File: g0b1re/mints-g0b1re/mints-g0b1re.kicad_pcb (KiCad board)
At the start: 2 copper layers, 2 parts

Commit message: Board updates
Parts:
- removed REF**: PinHeader_1x04_P2.54mm_Vertical, Connector_PinHeader_2.54mm:PinHeader_1x04_P2.54mm_Vertical
- removed REF**: TestPoint_Pad_D1.0mm, TestPoint:TestPoint_Pad_D1.0mm
- added C1: 10n, Capacitor_SMD:C_0603_1608Metric, F.Cu at (163.8, 153.3)
- added C10: 1u, Capacitor_SMD:C_0603_1608Metric, F.Cu at (163.8, 163.3)
- added C101: 1u, Capacitor_SMD:C_0603_1608Metric, F.Cu at (190.7, 142.8)
- added C102: 10u, Capacitor_SMD:C_0603_1608Metric, F.Cu at (190.7, 146.3)
- added C103: 1u, Capacitor_SMD:C_0603_1608Metric, F.Cu at (190.7, 149.8)
- added C104: 1u, Capacitor_SMD:C_0603_1608Metric, F.Cu at (194.7, 149.8)
- added C11: 10u, Capacitor_SMD:C_0603_1608Metric, F.Cu at (195.5, 118.6)
- added C12: 22u, Capacitor_SMD:C_0603_1608Metric, F.Cu at (189.0, 119.8)
- added C13: 0.1u, Capacitor_SMD:C_0603_1608Metric, F.Cu at (186.5, 115.2)
- added C14: 22u, Capacitor_SMD:C_0603_1608Metric, F.Cu at (198.5, 118.6)
- added C15: 0.1u, Capacitor_SMD:C_0603_1608Metric, F.Cu at (161.8, 108.9)
- added C16: 10n, Capacitor_SMD:C_0603_1608Metric, F.Cu at (163.8, 165.8)
- added C17: 10n, Capacitor_SMD:C_0603_1608Metric, F.Cu at (163.8, 168.3)
- added C18: 10n, Capacitor_SMD:C_0603_1608Metric, F.Cu at (163.8, 170.9)
- added C19: 10n, Capacitor_SMD:C_0603_1608Metric, F.Cu at (163.8, 173.4)
- added C2: 10n, Capacitor_SMD:C_0603_1608Metric, F.Cu at (163.8, 155.8)
- added C20: 22u, Capacitor_SMD:C_0603_1608Metric, F.Cu at (197.6, 173.3)
- added C3: 10n, Capacitor_SMD:C_0603_1608Metric, F.Cu at (163.8, 158.3)
- added C4: 10n, Capacitor_SMD:C_0603_1608Metric, F.Cu at (163.8, 160.8)
- added C5: 0.1u, Capacitor_SMD:C_0603_1608Metric, F.Cu at (164.3, 113.1)
- added C6: 0.1u, Capacitor_SMD:C_0603_1608Metric, F.Cu at (164.3, 107.1)
- added C7: 0.1u, Capacitor_SMD:C_0603_1608Metric, F.Cu at (161.8, 105.9)
- added C8: 1n, Capacitor_SMD:C_0603_1608Metric, F.Cu at (163.8, 126.0)
- added C9: 0.1u, Capacitor_SMD:C_0603_1608Metric, F.Cu at (166.8, 135.5)
- added D1: 3.3v, LED_SMD:LED_0603_1608Metric, F.Cu at (141.1, 76.3)
- added D101: 1SS396, Package_TO_SOT_SMD:SOT-23, F.Cu at (208.5, 187.2)
- added D102: 1SS396, Package_TO_SOT_SMD:SOT-23, F.Cu at (203.6, 187.2)
- added D103: 1SS396, Package_TO_SOT_SMD:SOT-23, F.Cu at (195.7, 187.2)
- added D104: 1SS396, Package_TO_SOT_SMD:SOT-23, F.Cu at (190.5, 187.2)
- added D105: 1SS396, Package_TO_SOT_SMD:SOT-23, F.Cu at (178.9, 187.2)
- added D106: 1SS396, Package_TO_SOT_SMD:SOT-23, F.Cu at (183.9, 187.2)
- added D107: 1SS396, Package_TO_SOT_SMD:SOT-23, F.Cu at (170.3, 187.2)
- added D108: 1SS396, Package_TO_SOT_SMD:SOT-23, F.Cu at (165.3, 187.2)
- added D2: LED, LED_SMD:LED_0603_1608Metric, F.Cu at (161.8, 114.9)
- added D201: SMBJ5360B-TP, Diode_SMD:D_SMB, F.Cu at (237.7, 85.1)
- added D202: SMBJ5360B-TP, Diode_SMD:D_SMB, F.Cu at (237.7, 119.1)
- added D203: SMBJ5360B-TP, Diode_SMD:D_SMB, F.Cu at (237.7, 151.8)
- added D204: SMBJ5360B-TP, Diode_SMD:D_SMB, F.Cu at (237.7, 185.3)
- added D205: red, LED_SMD:LED_0603_1608Metric, F.Cu at (197.1, 68.4)
- added D206: red, LED_SMD:LED_0603_1608Metric, F.Cu at (197.1, 71.2)
- added D207: red, LED_SMD:LED_0603_1608Metric, F.Cu at (197.1, 74.3)
- added D208: red, LED_SMD:LED_0603_1608Metric, F.Cu at (197.1, 77.3)
- added D209: red, LED_SMD:LED_0603_1608Metric, F.Cu at (201.0, 68.4)
- added D210: red, LED_SMD:LED_0603_1608Metric, F.Cu at (201.0, 71.3)
- added D211: red, LED_SMD:LED_0603_1608Metric, F.Cu at (201.0, 74.4)
- added D212: red, LED_SMD:LED_0603_1608Metric, F.Cu at (201.0, 77.4)
- added D213: SMBJ5360B-TP, Diode_SMD:D_SMB, F.Cu at (251.7, 97.8)
- added D214: SMBJ5360B-TP, Diode_SMD:D_SMB, F.Cu at (251.7, 131.6)
- added D215: SMBJ5360B-TP, Diode_SMD:D_SMB, F.Cu at (251.7, 163.8)
- added D216: SMBJ5360B-TP, Diode_SMD:D_SMB, F.Cu at (251.7, 197.3)
- added D217: red, LED_SMD:LED_0603_1608Metric, F.Cu at (141.1, 68.8)
- added D3: GREEN, LED_SMD:LED_0603_1608Metric, F.Cu at (183.5, 115.2)
- added F1: 350mA Poly, Fuse:Fuse_1206_3216Metric, F.Cu at (140.7, 132.6)
- added F201: 5x20 mm Fuse Holder, Fuse:Fuseholder_Cylinder-5x20mm_Schurter_0031_8201_Horizontal_Open, F.Cu at (146.1, 72.3)
- added H1: MountingHole, MountingHole:MountingHole_3.2mm_M3, F.Cu at (154.3, 86.0)
- added H2: MountingHole, MountingHole:MountingHole_3.2mm_M3, F.Cu at (154.3, 176.4)
- added H3: MountingHole, MountingHole:MountingHole_3.2mm_M3, F.Cu at (208.0, 176.4)
- added H4: MountingHole, MountingHole:MountingHole_3.2mm_M3, F.Cu at (202.5, 86.5)
- added J1: Conn_01x08, Connector_PinHeader_2.54mm:PinHeader_1x08_P2.54mm_Vertical, F.Cu at (141.3, 172.0)
- added J3: Conn_01x02, TerminalBlock_Phoenix:TerminalBlock_Phoenix_MKDS-1,5-2-5.08_1x02_P5.08mm_Horizontal, F.Cu at (183.3, 72.3)
- added J4: Conn_01x04, Connector_PinHeader_2.54mm:PinHeader_1x04_P2.54mm_Vertical, F.Cu at (141.3, 137.7)
- added J5: Conn_01x04, Connector_PinHeader_2.54mm:PinHeader_1x04_P2.54mm_Vertical, F.Cu at (141.3, 149.1)
- added J6: FTSH-107-01-X-DV-K, FTSH:SAMTEC_FTSH-107-01-X-DV-K, F.Cu at (165.8, 92.8)
- added J7: Conn_01x04, Connector_PinHeader_2.54mm:PinHeader_1x04_P2.54mm_Vertical, F.Cu at (141.3, 109.3)
- added L2: 4.7u, Inductor_SMD:L_1210_3225Metric, F.Cu at (191.5, 119.4)
- added Q1: SQM120P06-07L_GE3, SQM120P06-07L_GE3:TO-263_SQM120P06-07L_GE3_VIS, F.Cu at (235.8, 70.7)
- added Q2: SQM120P06-07L_GE3, SQM120P06-07L_GE3:TO-263_SQM120P06-07L_GE3_VIS, F.Cu at (249.8, 83.0)
- added Q3: SQM120P06-07L_GE3, SQM120P06-07L_GE3:TO-263_SQM120P06-07L_GE3_VIS, F.Cu at (235.8, 104.3)
- added Q4: SQM120P06-07L_GE3, SQM120P06-07L_GE3:TO-263_SQM120P06-07L_GE3_VIS, F.Cu at (235.8, 137.0)
- added Q5: SQM120P06-07L_GE3, SQM120P06-07L_GE3:TO-263_SQM120P06-07L_GE3_VIS, F.Cu at (249.8, 149.0)
- added Q6: SQM120P06-07L_GE3, SQM120P06-07L_GE3:TO-263_SQM120P06-07L_GE3_VIS, F.Cu at (235.8, 170.5)
- added Q7: SQM120P06-07L_GE3, SQM120P06-07L_GE3:TO-263_SQM120P06-07L_GE3_VIS, F.Cu at (249.8, 182.5)
- added Q8: SQM120P06-07L_GE3, SQM120P06-07L_GE3:TO-263_SQM120P06-07L_GE3_VIS, F.Cu at (249.8, 116.3)
- added R1: 100, Resistor_SMD:R_0603_1608Metric, F.Cu at (167.8, 153.3)
- added R10: 4k7, Resistor_SMD:R_0603_1608Metric, F.Cu at (167.8, 170.9)
- added R101: 1, Resistor_SMD:R_0603_1608Metric, F.Cu at (194.7, 142.8)
- added R102: 0, Resistor_SMD:R_0603_1608Metric, F.Cu at (194.7, 146.3)
- added R104: R_ADC_TOP, Resistor_SMD:R_0603_1608Metric, F.Cu at (204.0, 190.3)
- added R105: R_ADC_POS, Resistor_SMD:R_0603_1608Metric, F.Cu at (208.0, 190.3)
- added R106: R_ADC_BTM, Resistor_SMD:R_0603_1608Metric, F.Cu at (204.0, 193.3)
- added R107: R_ADC_NEG, Resistor_SMD:R_0603_1608Metric, F.Cu at (208.0, 193.3)
- added R108: R_ADC_TOP, Resistor_SMD:R_0603_1608Metric, F.Cu at (191.2, 190.3)
- added R109: R_ADC_POS, Resistor_SMD:R_0603_1608Metric, F.Cu at (195.3, 190.3)
- added R11: 4k7, Resistor_SMD:R_0603_1608Metric, F.Cu at (167.8, 173.4)
- added R110: R_ADC_BTM, Resistor_SMD:R_0603_1608Metric, F.Cu at (191.2, 193.3)
- added R111: R_ADC_NEG, Resistor_SMD:R_0603_1608Metric, F.Cu at (195.3, 193.3)
- added R112: R_ADC_TOP, Resistor_SMD:R_0603_1608Metric, F.Cu at (179.3, 190.3)
- added R113: R_ADC_POS, Resistor_SMD:R_0603_1608Metric, F.Cu at (183.3, 190.3)
- added R114: R_ADC_BTM, Resistor_SMD:R_0603_1608Metric, F.Cu at (179.3, 193.3)
- added R115: R_ADC_NEG, Resistor_SMD:R_0603_1608Metric, F.Cu at (183.3, 193.3)
- added R116: R_ADC_TOP, Resistor_SMD:R_0603_1608Metric, F.Cu at (169.7, 193.3)
- added R117: R_ADC_POS, Resistor_SMD:R_0603_1608Metric, F.Cu at (169.7, 196.3)
- added R118: R_ADC_BTM, Resistor_SMD:R_0603_1608Metric, F.Cu at (166.0, 190.3)
- added R119: R_ADC_NEG, Resistor_SMD:R_0603_1608Metric, F.Cu at (166.0, 193.3)
- added R12: 4k7, Resistor_SMD:R_0603_1608Metric, F.Cu at (171.8, 153.3)
- added R120: R_SHUNT, Resistor_SMD:R_0603_1608Metric, F.Cu at (204.0, 196.3)
- added R121: R_SHUNT, Resistor_SMD:R_0603_1608Metric, F.Cu at (191.2, 196.3)
- added R122: R_SHUNT, Resistor_SMD:R_0603_1608Metric, F.Cu at (179.3, 196.3)
- added R123: R_SHUNT, Resistor_SMD:R_0603_1608Metric, F.Cu at (169.7, 190.3)
- added R124: R_BIAS, Resistor_SMD:R_0603_1608Metric, F.Cu at (208.0, 196.3)
- added R125: R_BIAS, Resistor_SMD:R_0603_1608Metric, F.Cu at (195.3, 196.3)
- added R126: R_BIAS, Resistor_SMD:R_0603_1608Metric, F.Cu at (183.3, 196.3)
- added R127: R_BIAS, Resistor_SMD:R_0603_1608Metric, F.Cu at (166.0, 196.3)
- added R13: 4k7, Resistor_SMD:R_0603_1608Metric, F.Cu at (171.8, 155.8)
- added R14: 4k7, Resistor_SMD:R_0603_1608Metric, F.Cu at (171.8, 158.3)
- added R15: 0, Resistor_SMD:R_0603_1608Metric, F.Cu at (171.8, 160.8)
- added R16: 0, Resistor_SMD:R_0603_1608Metric, F.Cu at (171.8, 163.3)
- added R17: 0, Resistor_SMD:R_0603_1608Metric, F.Cu at (171.8, 165.8)
- added R18: 10k, Resistor_SMD:R_0603_1608Metric, F.Cu at (198.5, 115.4)
- added R19: 5k1, Resistor_SMD:R_0603_1608Metric, F.Cu at (186.5, 118.7)
- added R2: 100, Resistor_SMD:R_0603_1608Metric, F.Cu at (167.8, 155.8)
- added R20: 100, Resistor_SMD:R_0603_1608Metric, F.Cu at (171.8, 168.3)
- added R201: 4k7, Resistor_SMD:R_0603_1608Metric, F.Cu at (204.9, 68.4)
- added R202: 4k7, Resistor_SMD:R_0603_1608Metric, F.Cu at (205.0, 71.4)
- added R203: 4k7, Resistor_SMD:R_0603_1608Metric, F.Cu at (205.0, 74.4)
- added R204: 4k7, Resistor_SMD:R_0603_1608Metric, F.Cu at (204.9, 77.4)
- added R205: 4k7, Resistor_SMD:R_0603_1608Metric, F.Cu at (208.7, 77.4)
- added R206: 4k7, Resistor_SMD:R_0603_1608Metric, F.Cu at (208.8, 68.4)
- added R207: 4k7, Resistor_SMD:R_0603_1608Metric, F.Cu at (208.9, 71.4)
- added R208: 4k7, Resistor_SMD:R_0603_1608Metric, F.Cu at (208.9, 74.4)
- added R209: 47, Resistor_SMD:R_0603_1608Metric, F.Cu at (174.8, 70.8)
- added R21: 100, Resistor_SMD:R_0603_1608Metric, F.Cu at (171.8, 170.9)
- added R210: 240, Resistor_SMD:R_0603_1608Metric, F.Cu at (174.8, 73.3)
- added R22: 100, Resistor_SMD:R_0603_1608Metric, F.Cu at (171.8, 173.4)
- added R23: 100, Resistor_SMD:R_0603_1608Metric, F.Cu at (175.7, 153.3)
- added R24: 100, Resistor_SMD:R_0603_1608Metric, F.Cu at (175.9, 155.8)
- added R25: 100, Resistor_SMD:R_0603_1608Metric, F.Cu at (175.9, 158.3)
- added R26: 0, Resistor_SMD:R_0603_1608Metric, F.Cu at (175.9, 160.8)
- added R27: 0, Resistor_SMD:R_0603_1608Metric, F.Cu at (175.9, 163.3)
- added R28: 0, Resistor_SMD:R_0603_1608Metric, F.Cu at (175.9, 165.8)
- added R29: 5k1, Resistor_SMD:R_0603_1608Metric, F.Cu at (161.8, 111.9)
- added R3: 60.4, Resistor_SMD:R_0603_1608Metric, F.Cu at (169.8, 126.0)
- added R30: 510, Resistor_SMD:R_0603_1608Metric, F.Cu at (194.0, 173.3)
- added R31: 0, Resistor_SMD:R_0603_1608Metric, F.Cu at (190.7, 173.3)
- added R4: 60.4, Resistor_SMD:R_0603_1608Metric, F.Cu at (166.8, 126.0)
- added R5: 4k7, Resistor_SMD:R_0603_1608Metric, F.Cu at (167.8, 158.3)
- added R6: 4k7, Resistor_SMD:R_0603_1608Metric, F.Cu at (167.8, 160.8)
- added R7: 4k7, Resistor_SMD:R_0603_1608Metric, F.Cu at (167.8, 163.3)
- added R8: 4k7, Resistor_SMD:R_0603_1608Metric, F.Cu at (167.8, 165.8)
- added R9: 4k7, Resistor_SMD:R_0603_1608Metric, F.Cu at (167.8, 168.3)
- added RN201: 330, Resistor_SMD:R_Array_Convex_4x0603, F.Cu at (209.9, 98.8)
- added RN202: 330, Resistor_SMD:R_Array_Convex_4x0603, F.Cu at (209.9, 148.0)
- added RN203: 5k1, Resistor_SMD:R_Array_Convex_4x0603, F.Cu at (228.4, 92.5)
- added RN204: 5k1, Resistor_SMD:R_Array_Convex_4x0603, F.Cu at (229.3, 157.3)
- added SW1: SW_Coded_SH-7050, Button_Switch_THT:Nidec_Copal_SH-7010C, F.Cu at (141.0, 90.7)
- added TP1: TestPoint, oresat-misc:TestPoint-0.75mm-th, F.Cu at (195.5, 114.4)
- added TP2: TestPoint, oresat-misc:TestPoint-0.75mm-th, F.Cu at (198.5, 169.3)
- added TP201: TestPoint, TestPoint:TestPoint_Pad_D1.0mm, F.Cu at (198.5, 165.3)
- added U1: STM32G0B1RETx, Package_QFP:LQFP-64_10x10mm_P0.5mm, F.Cu at (190.7, 94.1)
- added U2: TCAN3414DDFR, TCAN3414DDFR(1):SOT65P280X110-8N, F.Cu at (166.7, 131.1)
- added U201: 140357145200, Package_SO:SO-4_4.4x3.6mm_P2.54mm, F.Cu at (219.3, 71.3)
- added U202: 140357145200, Package_SO:SO-4_4.4x3.6mm_P2.54mm, F.Cu at (219.3, 86.3)
- added U203: 140357145200, Package_SO:SO-4_4.4x3.6mm_P2.54mm, F.Cu at (219.3, 102.8)
- added U204: 140357145200, Package_SO:SO-4_4.4x3.6mm_P2.54mm, F.Cu at (219.3, 118.0)
- added U205: 140357145200, Package_SO:SO-4_4.4x3.6mm_P2.54mm, F.Cu at (219.3, 134.8)
- added U206: 140357145200, Package_SO:SO-4_4.4x3.6mm_P2.54mm, F.Cu at (219.3, 166.1)
- added U207: 140357145200, Package_SO:SO-4_4.4x3.6mm_P2.54mm, F.Cu at (219.3, 150.8)
- added U208: 140357145200, Package_SO:SO-4_4.4x3.6mm_P2.54mm, F.Cu at (219.3, 180.3)
- added U3: MCP3564R, Package_DFN_QFN:UQFN-20-1EP_3x3mm_P0.4mm_EP1.85x1.85mm, F.Cu at (194.0, 167.5)
- added U4: TCA9548, Package_DFN_QFN:Texas_RGE0024C_VQFN-24-1EP_4x4mm_P0.5mm_EP2.1x2.1mm, F.Cu at (169.8, 147.6)
- added U5: AP63203WU, Package_TO_SOT_SMD:TSOT-23-6, F.Cu at (191.5, 114.4)
- added U6: LM4040CIM3-2.0/NOPB, LM4040CIM3:DBZ3, F.Cu at (187.0, 167.8)
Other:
- board outline added: 119.5 x 139.5 mm

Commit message: polishing schematic, add variants, fix some small issues
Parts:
- removed J7: Conn_01x04, Connector_PinHeader_2.54mm:PinHeader_1x04_P2.54mm_Vertical
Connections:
- net EXTI renamed ADC_nIRQ
- net NRST renamed /NRST
- net SWCLK renamed /SWCLK
- net SWDIO renamed /SWDIO
- net VCP_RX renamed /VCP_RX
- net VCP_TX renamed /VCP_TX
- F1 pad 2: Net-(J4-Pin_3) -> Net-(J4-Pin_1)
- J4 pad 1: GND -> Net-(J4-Pin_1)
- J4 pad 2: GND -> CAN+
- J4 pad 3: Net-(J4-Pin_3) -> CAN-
- J4 pad 4: Net-(J4-Pin_3) -> GND
- J5 pad 1: CAN+ -> Net-(J4-Pin_1)
- J5 pad 4: CAN- -> GND
- U1 pad 18: CTRL -> unconnected-(U1-PA1-Pad18)
- U1 pad 25: CANTX -> /CAN_RXD
- U1 pad 26: CANRX -> /CAN_TXD
- U1 pad 36: unconnected-(U1-PA8-Pad36) -> SPI_nCS
- U2 pad 1: CANTX -> /CAN_TXD
- U2 pad 4: CANRX -> /CAN_RXD
- U3 pad 11: CTRL -> SPI_nCS

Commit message: handles merge conflicts
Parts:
- added J7: Conn_01x04, Connector_PinHeader_2.54mm:PinHeader_1x04_P2.54mm_Vertical, F.Cu at (111.1, 126.1)
- moved D215 173.9 mm to (79.4, 188.1), turned to 90 degrees
- moved D203 166.9 mm to (79.5, 205.0), turned to 90 degrees
- moved Q5 161.2 mm to (93.4, 188.1), turned to -90 degrees
- moved Q1 160.4 mm to (147.4, 204.5), turned to -90 degrees
- moved D201 158.7 mm to (133.4, 204.6), turned to 90 degrees
- moved Q4 157.8 mm to (93.5, 205.0), turned to -90 degrees
- moved D213 148.8 mm to (133.9, 188.7), turned to 90 degrees
- moved Q2 146.9 mm to (147.6, 188.5), turned to -90 degrees
- moved D216 145.4 mm to (106.5, 188.3), turned to 90 degrees
- moved D204 132.8 mm to (106.3, 204.9), turned to 90 degrees
- moved Q7 129.0 mm to (121.0, 188.5), turned to -90 degrees
- moved U201 128.7 mm to (130.7, 164.7), turned to -90 degrees
- moved C14 123.9 mm to (87.4, 173.4), turned to 180 degrees
- moved R18 122.5 mm to (90.6, 173.4), turned to 180 degrees
- moved RN203 121.8 mm to (138.7, 174.9), turned to -90 degrees
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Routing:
- net AUX_POW-: track 0.00 -> 297.4 mm, vias 0 -> 12
- net VPOW: track 0.00 -> 139.7 mm, vias 0 -> 6
- net +3V3: track 0.00 -> 136.0 mm, vias 0 -> 2
- net +3.3VA: track 0.00 -> 82.1 mm, vias 0 -> 9
- net /outputs/~{ISO_OUT_4}: track 0.00 -> 81.5 mm
- net /outputs/~{ISO_OUT_2}: track 0.00 -> 58.8 mm
- net /outputs/~{ISO_OUT_6}: track 0.00 -> 51.3 mm
- net /outputs/~{ISO_OUT_0}: track 0.00 -> 45.9 mm
- net /outputs/~{ISO_OUT_5}: track 0.00 -> 44.7 mm
- net OUT1/IN0-: track 0.00 -> 40.6 mm
- net CTRL: track 0.00 -> 40.4 mm
- net /outputs/~{ISO_OUT_3}: track 0.00 -> 38.6 mm
- net SPI_SCK: track 0.00 -> 38.6 mm
- net NRST: track 0.00 -> 37.4 mm, vias 0 -> 2
- net OUT7/IN3-: track 0.00 -> 37.2 mm
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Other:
- board outline removed

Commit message: Changed board stackup to OSH Park, added board variables
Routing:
- net NRST: track 37.4 -> 0.00 mm, vias 2 -> 0
- net /NRST: track 0.00 -> 37.4 mm, vias 0 -> 2
- net EXTI: track 18.0 -> 0.00 mm
- net ADC_nIRQ: track 0.00 -> 18.0 mm
- net SWDIO: track 17.9 -> 0.00 mm
- net /SWDIO: track 0.00 -> 17.9 mm

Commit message: board updates 9/2/26
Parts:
- removed C1, C16, C17, C18, C19, C2, C3, C4: 10n, Capacitor_SMD:C_0603_1608Metric
- removed J7: Conn_01x04, Connector_PinHeader_2.54mm:PinHeader_1x04_P2.54mm_Vertical
- added RN205: 5k1, Resistor_SMD:R_Array_Convex_4x0603, F.Cu at (138.5, 184.7)
- added RN206: 5k1, Resistor_SMD:R_Array_Convex_4x0603, F.Cu at (126.5, 184.7)
- J1: footprint Connector_PinHeader_2.54mm:PinHeader_1x08_P2.54mm_Vertical -> Connector_Phoenix_MSTB:PhoenixContact_MSTBA_2,5_8-G-5,08_1x08_P5.08mm_Horizontal
- J3: footprint TerminalBlock_Phoenix:TerminalBlock_Phoenix_MKDS-1,5-2-5.08_1x02_P5.08mm_Horizontal -> Connector_Phoenix_MSTB:PhoenixContact_MSTBA_2,5_2-G-5,08_1x02_P5.08mm_Horizontal
- J4, J5: footprint Connector_PinHeader_2.54mm:PinHeader_1x04_P2.54mm_Vertical -> Connector_Phoenix_MSTB:PhoenixContact_MSTBA_2,5_4-G-5,08_1x04_P5.08mm_Horizontal
- Q1, Q2, Q3, Q4, Q5, Q6, Q7, Q8: footprint SQM120P06-07L_GE3:TO-263_SQM120P06-07L_GE3_VIS -> LIB_DMP6023LFGQ-7:DMTH8008LFGQ7
- moved D217 118.1 mm to (94.3, 208.9)
- moved F201 115.3 mm to (108.5, 207.7), turned to 90 degrees
- moved R209 115.2 mm to (97.8, 208.9), turned to 180 degrees
- moved R210 110.2 mm to (94.3, 205.9)
- moved J3 109.8 mm to (87.0, 200.8), turned to -90 degrees
- moved D1 108.4 mm to (97.8, 205.9)
- moved H2 67.8 mm to (96.5, 187.7)
- moved H3 58.8 mm to (154.3, 187.1)
- moved R13 49.8 mm to (97.4, 155.8), turned to 0 degrees
- moved C10 46.4 mm to (111.2, 146.2), turned to 180 degrees
- moved R24 44.1 mm to (97.4, 153.0), turned to 180 degrees
- moved R5 42.8 mm to (111.2, 143.2), turned to 180 degrees
- moved R2 41.7 mm to (97.6, 110.8), turned to 180 degrees
- moved R28 41.7 mm to (108.0, 146.2), turned to 0 degrees
- moved D215 41.2 mm to (120.1, 194.8)
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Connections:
- Q1 pad 1: /outputs/~{ISO_OUT_0} -> Net-(Q1-G)
- Q2 pad 1: /outputs/~{ISO_OUT_1} -> Net-(Q2-G)
- Q3 pad 1: /outputs/~{ISO_OUT_2} -> unconnected-(Q3-G-Pad1)
- Q4 pad 1: /outputs/~{ISO_OUT_4} -> Net-(Q4-G)
- Q5 pad 1: /outputs/~{ISO_OUT_5} -> Net-(Q5-G)
- Q6 pad 1: /outputs/~{ISO_OUT_6} -> Net-(Q6-G)
- Q7 pad 1: /outputs/~{ISO_OUT_7} -> Net-(Q7-G)
- Q8 pad 1: /outputs/~{ISO_OUT_3} -> Net-(Q8-G)
- R3 pad 1: CAN + -> CAN+
- R4 pad 1: CAN - -> CAN-
- RN203 pad 5: /outputs/~{ISO_OUT_0} -> Net-(Q1-G)
- RN203 pad 6: /outputs/~{ISO_OUT_1} -> Net-(Q2-G)
- RN203 pad 7: /outputs/~{ISO_OUT_2} -> Net-(RN203B-R2.2)
- RN203 pad 8: /outputs/~{ISO_OUT_3} -> Net-(Q8-G)
- RN204 pad 5: /outputs/~{ISO_OUT_4} -> Net-(Q4-G)
- RN204 pad 6: /outputs/~{ISO_OUT_5} -> Net-(Q5-G)
- RN204 pad 7: /outputs/~{ISO_OUT_6} -> Net-(Q6-G)
- RN204 pad 8: /outputs/~{ISO_OUT_7} -> Net-(Q7-G)
- U2 pad 6: CAN + -> CAN+
- U2 pad 7: CAN - -> CAN-
- U203 pad 4: /outputs/~{ISO_OUT_2} -> AUX_POW-
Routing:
- net AUX_POW-: track 297.4 -> 136.1 mm, vias 12 -> 0
- net VPOW: track 139.7 -> 2.40 mm, vias 6 -> 0
- net +3V3: track 136.0 -> 270.2 mm
- net CAN-: track 0.00 -> 128.1 mm, vias 0 -> 2
- net CAN+: track 0.00 -> 124.0 mm, vias 0 -> 2
- net OUT5/IN2-: track 28.7 -> 136.7 mm, vias 0 -> 2
- net OUT4/IN2+: track 22.6 -> 130.6 mm, vias 0 -> 2
- net OUT3/IN1-: track 34.1 -> 139.8 mm, vias 0 -> 2
- net GNDA: track 8.12 -> 108.7 mm, vias 0 -> 4
- net OUT2/IN1+: track 31.2 -> 131.6 mm, vias 0 -> 2
- net OUT6/IN3+: track 24.7 -> 125.1 mm, vias 0 -> 2
- net OUT1/IN0-: track 40.6 -> 139.5 mm, vias 0 -> 2
- net OUT0/IN0+: track 37.1 -> 133.8 mm, vias 0 -> 2
- net OUT7/IN3-: track 37.2 -> 127.8 mm, vias 0 -> 2
- net /outputs/~{ISO_OUT_4}: track 81.5 -> 0.00 mm
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- added copper zone on F.Cu, net GND
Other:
- board outline added: 102.5 x 110 mm
- board text added: "R126"

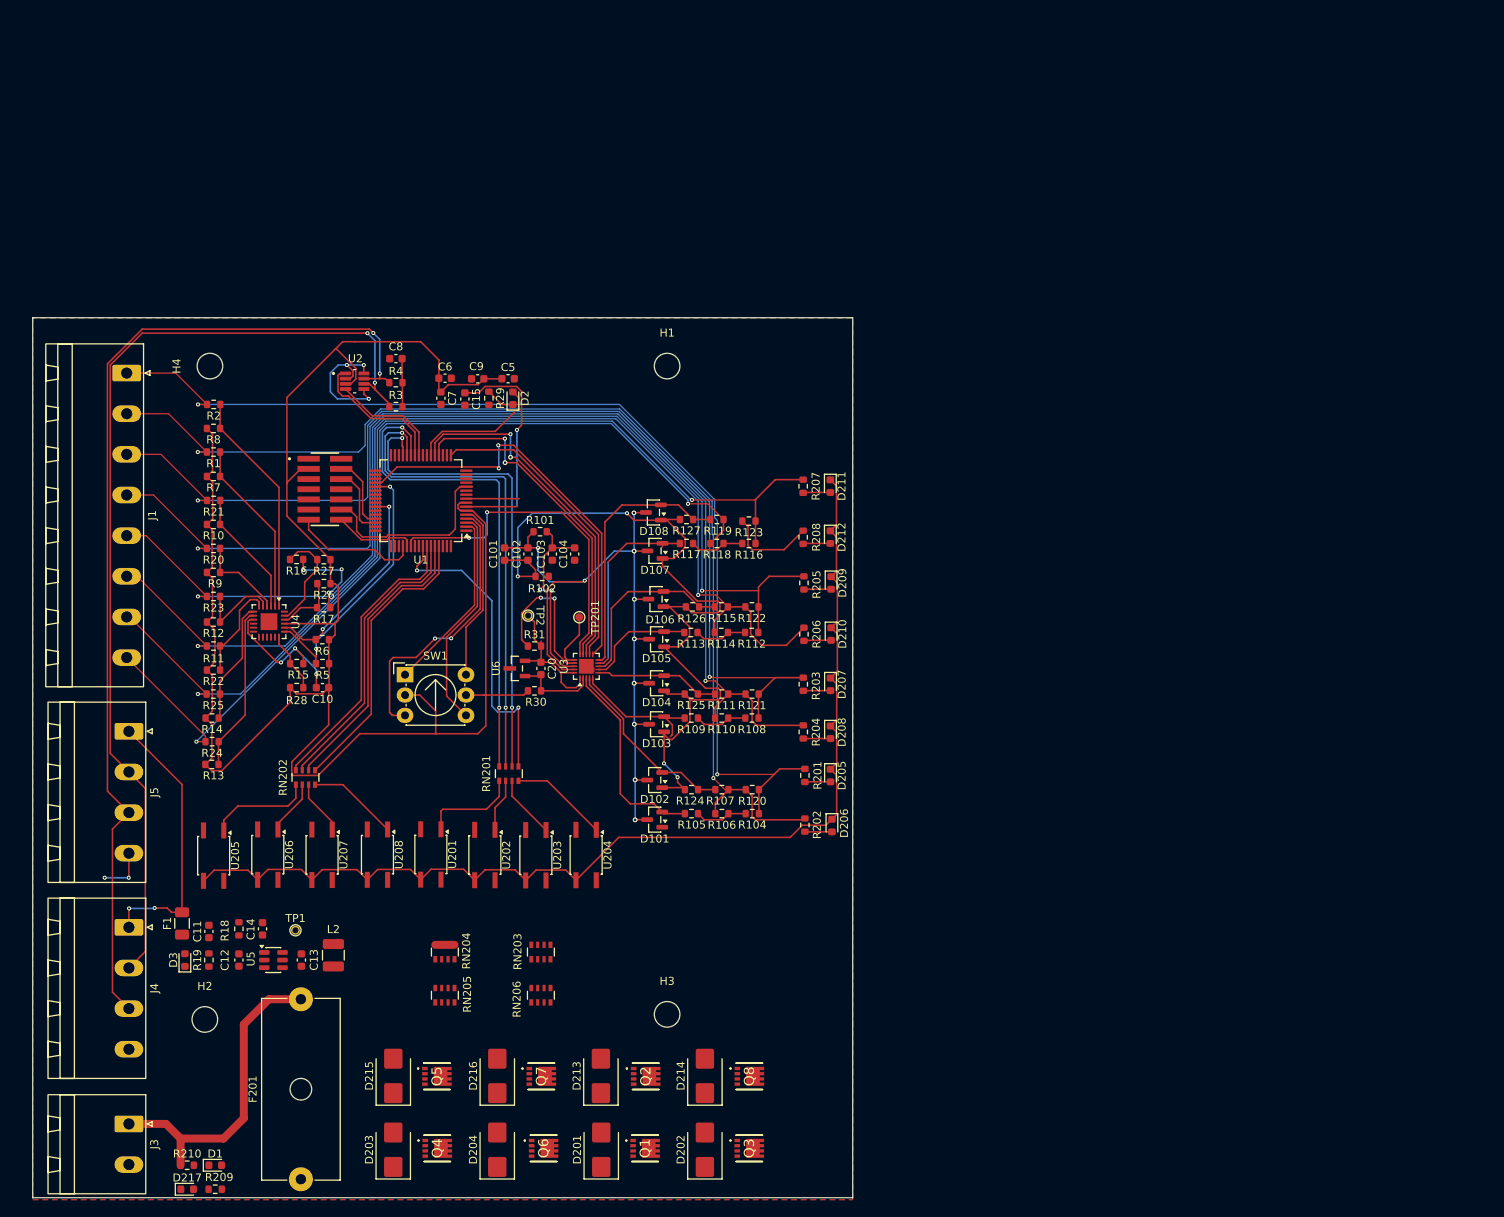
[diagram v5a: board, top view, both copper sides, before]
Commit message: finneshed trace routing; fixed DRC errors
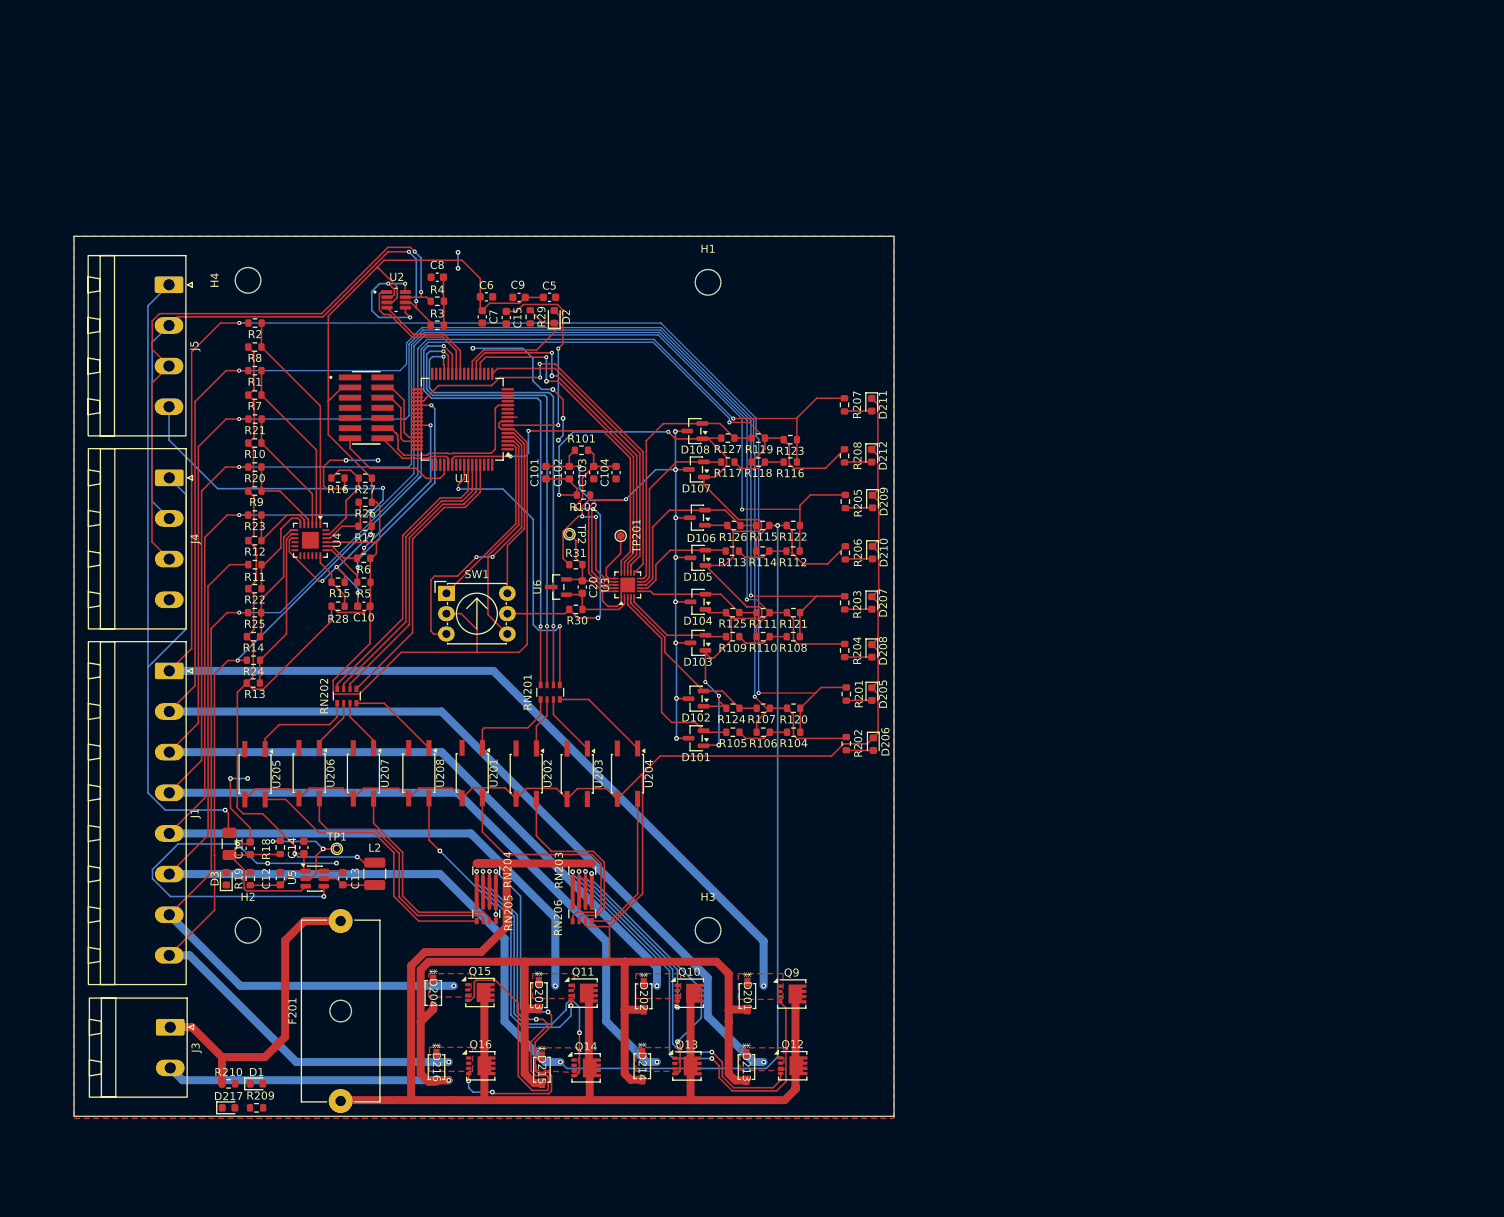
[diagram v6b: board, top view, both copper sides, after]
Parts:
- removed Q1, Q2, Q3, Q4, Q5, Q6, Q7, Q8: SQM120P06-07L_GE3, LIB_DMP6023LFGQ-7:DMTH8008LFGQ7
- added Q10: DMP3013SFV, Package_SON:Diodes_PowerDI3333-8, F.Cu at (157.1, 184.4)
- added Q11: DMP3013SFV, Package_SON:Diodes_PowerDI3333-8, F.Cu at (143.8, 184.4)
- added Q12: DMP3013SFV, Package_SON:Diodes_PowerDI3333-8, F.Cu at (170.0, 193.5)
- added Q13: DMP3013SFV, Package_SON:Diodes_PowerDI3333-8, F.Cu at (156.8, 193.5)
- added Q14: DMP3013SFV, Package_SON:Diodes_PowerDI3333-8, F.Cu at (144.2, 193.8)
- added Q15: DMP3013SFV, Package_SON:Diodes_PowerDI3333-8, F.Cu at (130.9, 184.3)
- added Q16: DMP3013SFV, Package_SON:Diodes_PowerDI3333-8, F.Cu at (131.0, 193.5)
- added Q9: DMP3013SFV, Package_SON:Diodes_PowerDI3333-8, F.Cu at (169.9, 184.5)
- D201, D202, D203, D204, D213, D214, D215, D216: footprint Diode_SMD:D_SMB -> SZMMSZ5258BT3G:SOD-123_ONS
- moved J4 56.4 mm to (92.1, 120.0)
- moved J5 56.0 mm to (92.0, 95.9)
- moved J1 37.6 mm to (92.1, 144.1)
- moved D203 26.5 mm to (138.3, 184.7), turned to -90 degrees
- moved D201 26.5 mm to (164.3, 184.8), turned to -90 degrees
- moved D204 21.2 mm to (125.1, 184.4), turned to -90 degrees
- moved D202 20.6 mm to (151.4, 184.8), turned to -90 degrees
- moved D215 18.6 mm to (138.7, 194.0), turned to -90 degrees
- moved D213 18.2 mm to (164.2, 193.7), turned to -90 degrees
- moved J3 13.1 mm to (92.2, 188.7)
- moved H2 12.4 mm to (101.9, 176.6)
- moved H4 11.7 mm to (101.9, 95.3)
- moved H3 11.7 mm to (159.4, 176.6)
- moved H1 11.7 mm to (159.4, 95.6)
- moved C11 11.6 mm to (102.2, 166.3)
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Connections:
- J3 pad 2: AU_POW - -> AUX_POW-
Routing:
- net AUX_POW-: track 136.1 -> 313.9 mm, vias 0 -> 1
- net VPOW: track 2.40 -> 165.8 mm
- net OUT0/IN0+: track 133.8 -> 264.4 mm, vias 2 -> 3
- net OUT1/IN0-: track 139.5 -> 269.9 mm, vias 2 -> 3
- net GND: track 79.8 -> 205.2 mm, vias 13 -> 26
- net OUT3/IN1-: track 139.8 -> 253.1 mm, vias 2 -> 3
- net OUT2/IN1+: track 131.6 -> 239.8 mm, vias 2 -> 3
- net OUT4/IN2+: track 130.6 -> 223.0 mm, vias 2 -> 3
- net OUT5/IN2-: track 136.7 -> 221.3 mm
- net OUT7/IN3-: track 127.8 -> 197.7 mm, vias 2 -> 3
- net Net-(J4-Pin_1): track 34.6 -> 104.3 mm, vias 2 -> 1
- net OUT6/IN3+: track 125.1 -> 192.6 mm, vias 2 -> 3
- net +3V3: track 270.2 -> 337.3 mm, vias 2 -> 5
- net Net-(Q15-G): track 0.00 -> 62.0 mm, vias 0 -> 2
- net Net-(Q9-G): track 0.00 -> 60.3 mm, vias 0 -> 2
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- added copper zone on F.Cu, net OUT0/IN0+
- added copper zone on F.Cu, net OUT1/IN0-
- added copper zone on F.Cu, net OUT2/IN1+
- added copper zone on F.Cu, net OUT3/IN1-
- added copper zone on F.Cu, net OUT4/IN2+
- added copper zone on F.Cu, net OUT5/IN2-
- added copper zone on F.Cu, net OUT6/IN3+
- added copper zone on F.Cu, net OUT7/IN3-
